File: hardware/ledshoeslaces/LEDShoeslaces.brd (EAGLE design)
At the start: 50 x 38 mm, 13 parts, among them IC1 LM1117MPX-5.0

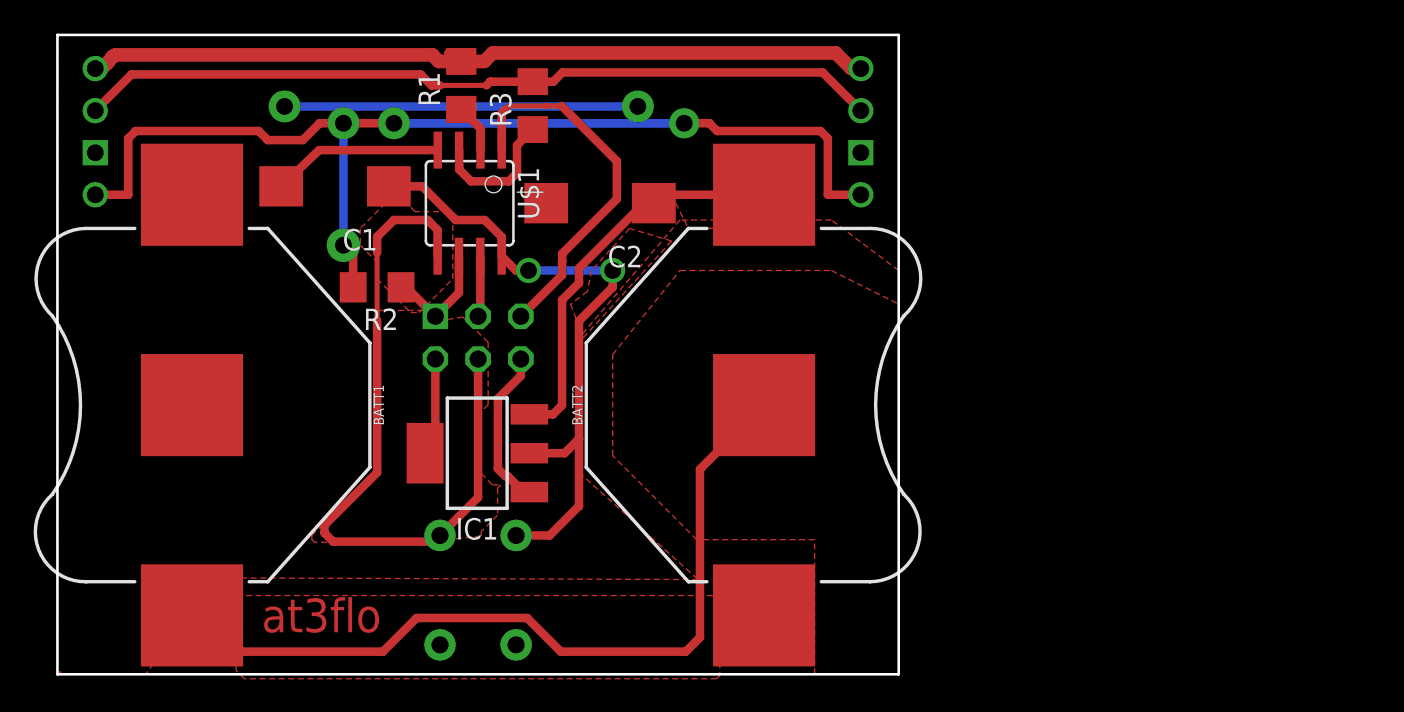
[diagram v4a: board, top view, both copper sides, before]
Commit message: rasnet fix cc with ground
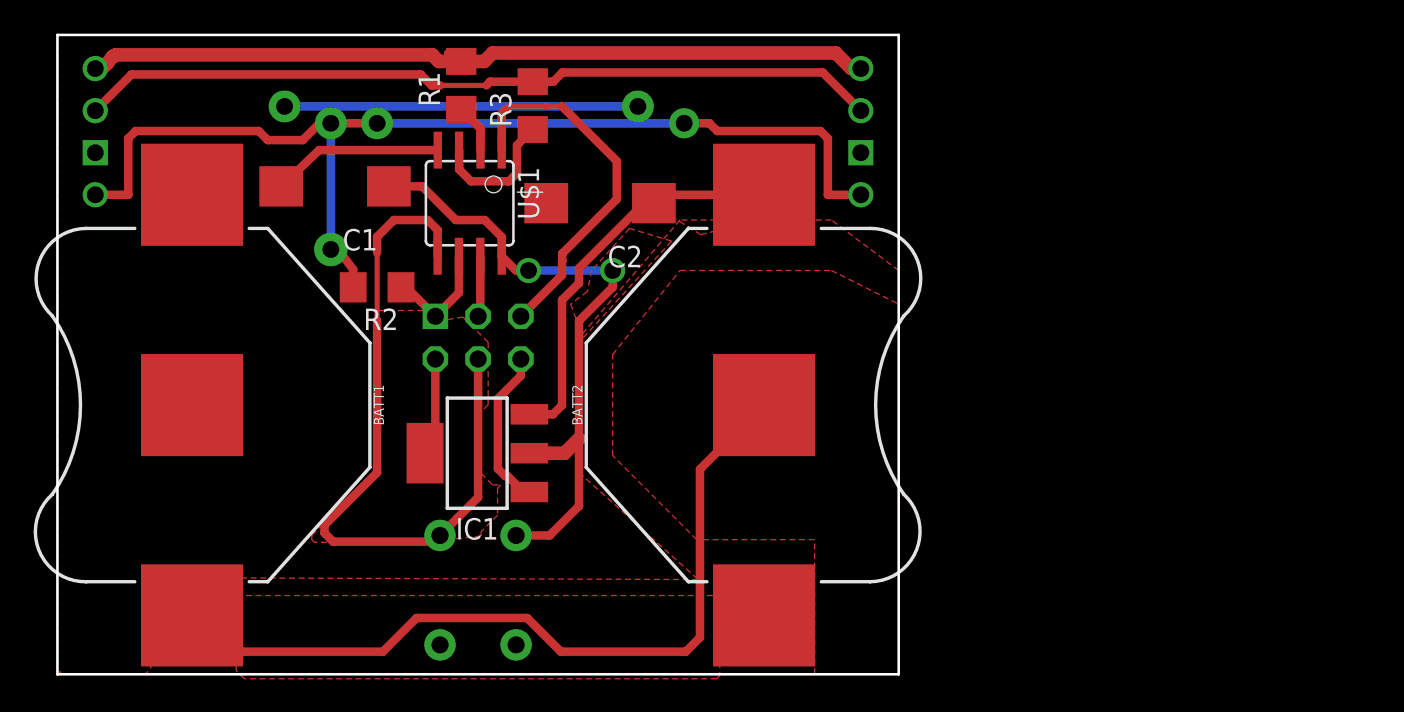
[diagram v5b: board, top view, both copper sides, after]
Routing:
- net ARED: track 63.4 -> 64.5 mm
- removed copper zone on layer 1, net MOSI
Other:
- board text removed: "at3flo"
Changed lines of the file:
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@@
 <setting verticaltext="up"/>
 </settings>
-<grid distance="0.25" unitdist="mm" unit="mm" style="lines" multiple="1" display="yes" altdistance="5" altunitdist="mil" altunit="mm"/>
+<grid distance="0.25" unitdist="mm" unit="mm" style="lines" multiple="1" display="no" altdistance="5" altunitdist="mil" altunit="mm"/>
 <layers>
 <layer number="1" name="Top" color="4" fill="1" visible="yes" active="yes"/>
@@
 <rectangle x1="0.183940625" y1="0.178859375" x2="0.18859375" y2="0.17928125" layer="1"/>
 <text x="0" y="-0.002115625" size="0.000846875" layer="1" font="vector">/ws/ng2017/assets/img/logo-600x600.bmp</text>
-<text x="13.25" y="3.5" size="0.000846875" layer="1" font="vector">at3flo</text>
-<text x="19.25" y="4.5" size="2" layer="1" font="vector" rot="R180">at3flo</text>
 <text x="78" y="14.25" size="0.000846875" layer="1" font="vector">numerik games 2017</text>
 </plain>
@@
 <vertex x="34" y="26.5"/>
 </polygon>
-<wire x1="28.049" y1="13.14" x2="30.14" y2="13.14" width="0.508" layer="1"/>
-<wire x1="30.14" y1="13.14" x2="31" y2="14" width="0.508" layer="1"/>
+<wire x1="28.049" y1="13.14" x2="30.14" y2="13.14" width="0.8128" layer="1"/>
+<wire x1="30.14" y1="13.14" x2="31" y2="14" width="0.8128" layer="1"/>
 <wire x1="22.46188125" y1="13.75088125" x2="28.049" y2="13.14" width="0" layer="19" extent="1-1"/>
 </signal>
@@
 <wire x1="25.00188125" y1="18.736903125" x2="25.00188125" y2="10.516296875" width="0.508" layer="1"/>
 <wire x1="19" y1="21.04174375" x2="19" y2="25.0575625" width="0.3048" layer="1"/>
-<polygon width="0.508" layer="1">
-<vertex x="20.75" y="28"/>
-<vertex x="19.5" y="28"/>
-<vertex x="18" y="26.5"/>
-<vertex x="18" y="25.5"/>
-<vertex x="19" y="24.5"/>
-<vertex x="19" y="23.5"/>
-<vertex x="21" y="21.5"/>
-<vertex x="21.5" y="21.5"/>
-<vertex x="23.5" y="23.5"/>
-<vertex x="23.5" y="27.25"/>
-<vertex x="23.25" y="27.5"/>
-<vertex x="21.25" y="27.5"/>
-</polygon>
 </signal>
 <signal name="MISO">
@@
 <wire x1="29.992" y1="15.992" x2="29.992" y2="22.245325" width="0.508" layer="1"/>
 <polygon width="0.508" layer="1">
-<vertex x="36.5" y="28.5"/>
-<vertex x="37.5" y="26.5"/>
-<vertex x="39.5" y="26.5"/>
-<vertex x="39.75" y="28.25"/>
+<vertex x="34.548" y="28.429"/>
+<vertex x="38.238" y="26.13"/>
+<vertex x="43.311" y="27.409"/>
+<vertex x="42.418" y="28.612"/>
 </polygon>
 </signal>
@@
 <signal name="ARED">
 <contactref element="R2" pad="2"/>
-<via x="17" y="32.75" extent="1-16" drill="1" diameter="1.9"/>
-<wire x1="17" y1="32.75" x2="17" y2="25.5" width="0.508" layer="16"/>
-<via x="17" y="25.5" extent="1-16" drill="1" diameter="2"/>
-<wire x1="20" y1="32.75" x2="17" y2="32.75" width="0.508" layer="1"/>
-<via x="20" y="32.75" extent="1-16" drill="1" diameter="1.9"/>
-<wire x1="20" y1="32.75" x2="37.25" y2="32.75" width="0.508" layer="16"/>
+<via x="16.25" y="32.75" extent="1-16" drill="1" diameter="1.9"/>
+<wire x1="16.25" y1="32.75" x2="16.25" y2="25.25" width="0.508" layer="16"/>
+<via x="16.25" y="25.25" extent="1-16" drill="1" diameter="2"/>
+<wire x1="16.25" y1="32.75" x2="19" y2="32.75" width="0.508" layer="1"/>
+<via x="19" y="32.75" extent="1-16" drill="1" diameter="1.9"/>
+<wire x1="19" y1="32.75" x2="37.25" y2="32.75" width="0.508" layer="16"/>
 <via x="37.25" y="32.75" extent="1-16" drill="1" diameter="1.8"/>
-<wire x1="17.578" y1="23" x2="17.578" y2="24.922" width="0.508" layer="1"/>
-<wire x1="17.578" y1="24.922" x2="17" y2="25.5" width="0.508" layer="1"/>
 <contactref element="U$3" pad="1"/>
 <contactref element="U$4" pad="1"/>
+<wire x1="16.329640625" y1="25.717425" x2="16.25" y2="25.25" width="0.508" layer="1"/>
 <wire x1="2.25" y1="28.5" x2="4.211" y2="28.5" width="0.508" layer="1"/>
 <wire x1="4.211" y1="28.5" x2="4.211" y2="31.84731875" width="0.508" layer="1"/>
 <wire x1="4.211" y1="31.84731875" x2="4.65268125" y2="32.289" width="0.508" layer="1"/>
-<wire x1="15.5834" y1="32.75" x2="17" y2="32.75" width="0.508" layer="1"/>
+<wire x1="15.5834" y1="32.75" x2="16.25" y2="32.75" width="0.508" layer="1"/>
 <wire x1="38.75" y1="32.75" x2="37.25" y2="32.75" width="0.508" layer="1"/>
 <wire x1="47.75" y1="28.5" x2="45.789" y2="28.5" width="0.508" layer="1"/>
@@
 <wire x1="14.5834" y1="31.75" x2="15.5834" y2="32.75" width="0.508" layer="1"/>
 <wire x1="4.65268125" y1="32.289" x2="11.961" y2="32.289" width="0.508" layer="1"/>
+<wire x1="17.578" y1="23" x2="17.578" y2="24.059784375" width="0.508" layer="1"/>
+<wire x1="17.578" y1="24.059784375" x2="16.329640625" y2="25.717425" width="0.508" layer="1"/>
 </signal>
 <signal name="AGRN">
